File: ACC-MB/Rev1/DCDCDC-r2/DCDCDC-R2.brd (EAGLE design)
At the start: 89.8 x 62 mm, 21 parts, among them X2 5566-4

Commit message: update
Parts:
- removed DCM290P138T600A40: 600W 400 to 12V, ACC-MB-R0:VICOR_CHIP_HEATSINK
- added U$8: VICOR_CHIP_WITH_HEATSINK, ACC-MB-R0:VICOR_CHIP_HEATSINK
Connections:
- net DCDC_OUT: now also U$8.OUT+_1, U$8.OUT+_2; no longer DCM290P138T600A40.OUT+_1, DCM290P138T600A40.OUT+_2
- net GND: now also U$8.OUT-_1, U$8.OUT-_2; no longer DCM290P138T600A40.OUT-_1, DCM290P138T600A40.OUT-_2
- net N$3: now also U$8.IN+; no longer DCM290P138T600A40.IN+
- net V-: now also U$8.IN-; no longer DCM290P138T600A40.IN-
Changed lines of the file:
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@@
 </layers>
 <board>
-<fusionsync huburn="a.YnVzaW5lc3M6bXl1d28yNA" projecturn="a.YnVzaW5lc3M6bXl1d28yNCNEMjAxOTA5MTgyMTU4NTEzMzE" f3durn="urn:adsk.wipprod:dm.lineage:U_-0G6fwRzqBO_3Lu0JAiA" pcbguid="ece931dd-8bcb-4325-baf8-111b939a3e73" lastpulledtime="" lastsyncedchangeguid="07639025-2a20-f54b-1a95-872b400ec342"/>
+<fusionsync huburn="a.YnVzaW5lc3M6bXl1d28yNA" projecturn="a.YnVzaW5lc3M6bXl1d28yNCNEMjAxOTA5MTgyMTU4NTEzMzE" f3durn="urn:adsk.wipprod:dm.lineage:U_-0G6fwRzqBO_3Lu0JAiA" pcbguid="ece931dd-8bcb-4325-baf8-111b939a3e73" lastpulledtime="" lastsyncedchangeguid="cb0f9be5-9551-2798-ee30-78990f0e4cb6"/>
 <plain>
 <wire x1="92.5" y1="66.5" x2="2.75" y2="66.5" width="0" layer="20"/>
@@
 </autorouter>
 <elements>
-<element name="DCM290P138T600A40" library="ACC-MB-R0" library_urn="urn:adsk.eagle:library:13324935" package="VICOR_CHIP_HEATSINK" package3d_urn="urn:adsk.eagle:package:13209498/1" value="600W 400 to 12V" x="44.35" y="48" smashed="yes" rot="R180">
-<attribute name="NAME" x="25.45" y="57.57" size="1.27" layer="21" rot="R270"/>
-<attribute name="VALUE" x="28.28" y="54.57" size="1.27" layer="21" rot="R270"/>
-</element>
 <element name="U$4" library="ACC-MB-R0" library_urn="urn:adsk.eagle:library:13324935" package="SOT23" package3d_urn="urn:adsk.eagle:package:13209499/1" value="RK7002BMT116" x="44.4" y="11.45" smashed="yes">
 <attribute name="NAME" x="42.495" y="13.355" size="1.27" layer="25"/>
@@
 <attribute name="SPICEPREFIX" value="R" x="7" y="42.5" size="1.778" layer="28" rot="MR270" display="off"/>
 </element>
+<element name="U$8" library="ACC-MB-R0" library_urn="urn:adsk.eagle:library:13208985" package="VICOR_CHIP_HEATSINK" package3d_urn="urn:adsk.eagle:package:13209498/2" value="VICOR_CHIP_WITH_HEATSINK" x="44.5" y="48" rot="R180"/>
 </elements>
 <signals>
@@
 <contactref element="R2" pad="1"/>
 <contactref element="U$5" pad="2"/>
-<contactref element="DCM290P138T600A40" pad="OUT-_1"/>
-<contactref element="DCM290P138T600A40" pad="OUT-_2"/>
 <polygon width="1" layer="16">
 <vertex x="53" y="-10.5"/>
@@
 <contactref element="U$2" pad="5"/>
 <contactref element="R4" pad="1"/>
+<contactref element="U$8" pad="OUT-_1"/>
+<contactref element="U$8" pad="OUT-_2"/>
+<wire x1="7" y1="43.45" x2="7.69" y2="58" width="0" layer="19" extent="16-16"/>
+<wire x1="5.6" y1="20.25" x2="7" y2="43.45" width="0" layer="19" extent="16-16"/>
+<wire x1="9.8" y1="20.25" x2="5.6" y2="20.25" width="0" layer="19" extent="1-1"/>
+<wire x1="14" y1="20.25" x2="9.8" y2="20.25" width="0" layer="19" extent="1-1"/>
+<wire x1="18.2" y1="20.25" x2="14" y2="20.25" width="0" layer="19" extent="1-1"/>
+<wire x1="22.4" y1="20.25" x2="18.2" y2="20.25" width="0" layer="19" extent="1-1"/>
+<wire x1="28.4" y1="6.75" x2="22.4" y2="20.25" width="0" layer="19" extent="1-1"/>
+<wire x1="32.6" y1="6.75" x2="28.4" y2="6.75" width="0" layer="19" extent="1-1"/>
+<wire x1="41.2" y1="10.4" x2="32.6" y2="6.75" width="0" layer="19" extent="1-1"/>
+<wire x1="21.31" y1="45.25" x2="28.4" y2="6.75" width="0" layer="19" extent="1-1"/>
+<wire x1="21.31" y1="56.25" x2="21.31" y2="45.25" width="0" layer="19" extent="1-1"/>
 </signal>
 <signal name="V+" class="1">
@@
 <contactref element="CFILTER_1" pad="P$2"/>
 <contactref element="CFILTER_2" pad="P$2"/>
-<contactref element="DCM290P138T600A40" pad="IN-"/>
 <wire x1="73.075" y1="63.925" x2="74.75" y2="63.925" width="1" layer="1"/>
-<wire x1="67.54" y1="56" x2="67.54" y2="60.96" width="3" layer="1"/>
 <wire x1="67.54" y1="60.96" x2="67.5" y2="61" width="3" layer="1"/>
 <wire x1="67.5" y1="61" x2="70.425" y2="63.925" width="3" layer="1"/>
 <wire x1="70.425" y1="63.925" x2="74.75" y2="63.925" width="3" layer="1"/>
 <wire x1="74.75" y1="63.925" x2="86" y2="63.925" width="3" layer="1"/>
-<wire x1="65" y1="56" x2="67.54" y2="56" width="3" layer="16"/>
 <wire x1="65.5" y1="35.5" x2="62" y2="39" width="3" layer="16"/>
 <wire x1="62" y1="39" x2="62" y2="53" width="3" layer="16"/>
-<wire x1="62" y1="53" x2="65" y2="56" width="3" layer="16"/>
+<wire x1="65" y1="56" x2="62" y2="53" width="3" layer="16"/>
 <contactref element="U$1" pad="4"/>
 <contactref element="U$1" pad="5"/>
@@
 <wire x1="64.8" y1="32.25980625" x2="65.5" y2="32.95980625" width="3" layer="16"/>
 <wire x1="65.5" y1="32.95980625" x2="65.5" y2="35.5" width="3" layer="16"/>
+<contactref element="U$8" pad="IN-"/>
+<wire x1="67.69" y1="56" x2="67.5" y2="56.19" width="3" layer="1"/>
+<wire x1="67.5" y1="56.19" x2="67.5" y2="61" width="3" layer="1"/>
+<wire x1="67.69" y1="56" x2="65" y2="56" width="3" layer="16"/>
 </signal>
 <signal name="+12V" class="1">
@@
 <signal name="N$3" class="1">
 <contactref element="L_IN" pad="P$2"/>
-<contactref element="DCM290P138T600A40" pad="IN+"/>
 <contactref element="CFILTER_1" pad="P$1"/>
 <contactref element="CFILTER_2" pad="P$1"/>
@@
 <wire x1="74.42" y1="51" x2="74.42" y2="41.095" width="3" layer="1"/>
 <wire x1="74.42" y1="41.095" x2="72.325" y2="39" width="3" layer="1"/>
-<wire x1="72.325" y1="39" x2="68.54" y2="39" width="3" layer="1"/>
-<wire x1="68.54" y1="39" x2="67.54" y2="40" width="3" layer="1"/>
+<wire x1="68.54" y1="39" x2="72.325" y2="39" width="3" layer="1"/>
+<contactref element="U$8" pad="IN+"/>
+<wire x1="67.69" y1="40" x2="67.69" y2="39.85" width="3" layer="1"/>
+<wire x1="67.69" y1="39.85" x2="68.54" y2="39" width="3" layer="1"/>
 </signal>
 <signal name="V+_FUSED" class="1">
@@
 </signal>
 <signal name="DCDC_OUT" class="1">
-<contactref element="DCM290P138T600A40" pad="OUT+_1"/>
-<contactref element="DCM290P138T600A40" pad="OUT+_2"/>
 <contactref element="COUT_EXT" pad="+"/>
 <polygon width="1" layer="1">
@@
 <contactref element="U$3" pad="1"/>
 <contactref element="U$3" pad="3"/>
+<contactref element="U$8" pad="OUT+_1"/>
+<contactref element="U$8" pad="OUT+_2"/>
+<wire x1="48.405" y1="25.215" x2="51.2" y2="26.3" width="0" layer="19" extent="1-1"/>
+<wire x1="47.135" y1="25.215" x2="48.405" y2="25.215" width="0" layer="19" extent="1-1"/>
+<wire x1="45.865" y1="25.215" x2="47.135" y2="25.215" width="0" layer="19" extent="1-1"/>
+<wire x1="40.905" y1="25.215" x2="45.865" y2="25.215" width="0" layer="19" extent="1-1"/>
+<wire x1="39.635" y1="25.215" x2="40.905" y2="25.215" width="0" layer="19" extent="1-1"/>
+<wire x1="38.365" y1="25.215" x2="39.635" y2="25.215" width="0" layer="19" extent="1-1"/>
+<wire x1="33.905" y1="25.215" x2="38.365" y2="25.215" width="0" layer="19" extent="1-1"/>
+<wire x1="32.635" y1="25.215" x2="33.905" y2="25.215" width="0" layer="19" extent="1-1"/>
+<wire x1="31.365" y1="25.215" x2="32.635" y2="25.215" width="0" layer="19" extent="1-1"/>
+<wire x1="15.31" y1="58" x2="31.365" y2="25.215" width="0" layer="19" extent="1-1"/>
+<wire x1="21.31" y1="39.75" x2="31.365" y2="25.215" width="0" layer="19" extent="1-1"/>
+<wire x1="21.31" y1="50.75" x2="21.31" y2="39.75" width="0" layer="19" extent="1-1"/>
 </signal>
 <signal name="N$4" class="1">

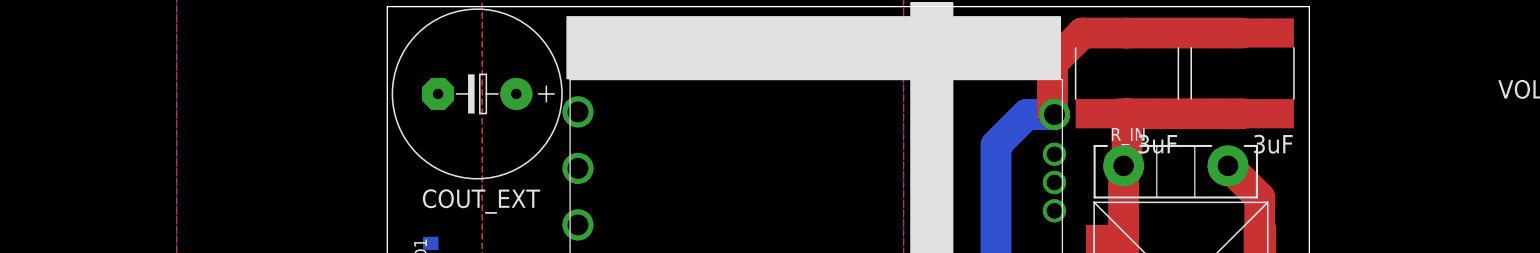
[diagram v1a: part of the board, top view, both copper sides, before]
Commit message: 7792 added to all DC
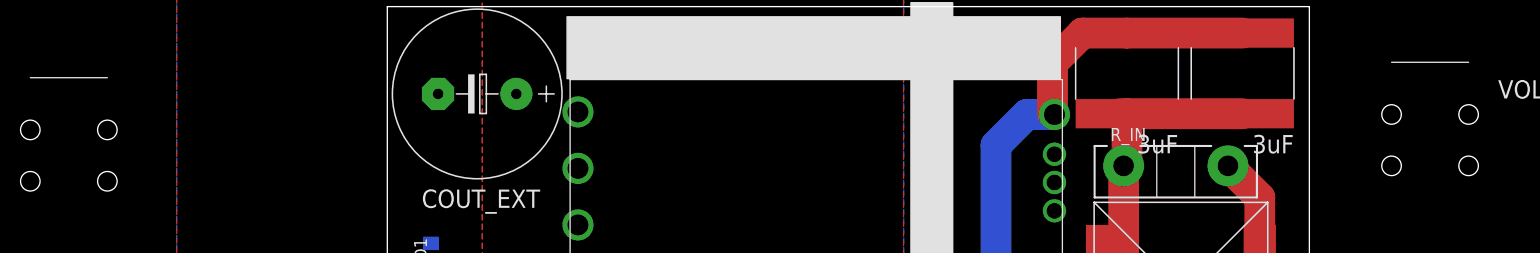
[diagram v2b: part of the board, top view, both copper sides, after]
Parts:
- added U$10, U$9: 7792, ACC-MB-R0:7792
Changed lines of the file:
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@@
 <drawing>
 <settings>
-<setting alwaysvectorfont="yes"/>
+<setting alwaysvectorfont="no"/>
 <setting verticaltext="up"/>
 </settings>
@@
 <vertex x="57.75" y="66.85"/>
 </polygon>
-<dimension x1="99.25" y1="75" x2="0.25" y2="75" x3="49.75" y3="80.5" textsize="1.778" layer="20"/>
 <wire x1="2.75" y1="4.5" x2="92.5" y2="4.5" width="0" layer="20"/>
 <wire x1="2.75" y1="66.5" x2="2.75" y2="4.5" width="0" layer="20"/>
@@
 </element>
 <element name="U$8" library="ACC-MB-R0" library_urn="urn:adsk.eagle:library:13208985" package="VICOR_CHIP_HEATSINK" package3d_urn="urn:adsk.eagle:package:13209498/2" value="VICOR_CHIP_WITH_HEATSINK" x="44.5" y="48" rot="R180"/>
+<element name="U$9" library="ACC-MB-R0" library_urn="urn:adsk.eagle:library:13208985" package="7792" package3d_urn="urn:adsk.eagle:package:14511284/2" value="7792" x="-32" y="49.5"/>
+<element name="U$10" library="ACC-MB-R0" library_urn="urn:adsk.eagle:library:13208985" package="7792" package3d_urn="urn:adsk.eagle:package:14511284/2" value="7792" x="100.5" y="51"/>
 </elements>
 <signals>
